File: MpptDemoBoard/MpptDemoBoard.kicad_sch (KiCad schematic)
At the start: 17 parts, among them IC1 SPV1040T, U1 282837-2, U2 282837-2

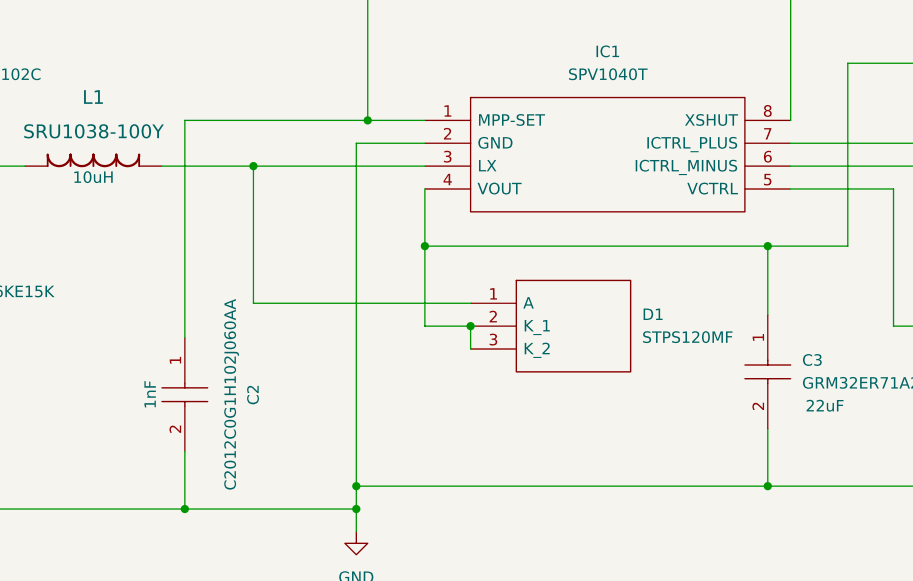
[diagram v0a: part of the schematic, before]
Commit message: Updated pcb with new diode
replaced diode STPS120MF (If=1A) with STPS2150A (If=2A). Updated symbol and footprint library and docs containing schematic, pcb layout image and 3d image.
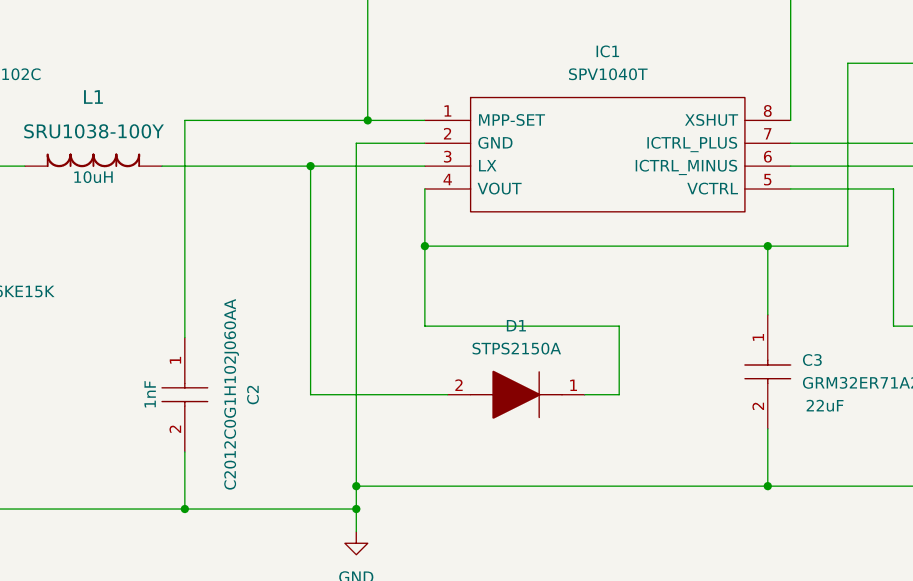
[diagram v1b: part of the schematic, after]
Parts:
- removed D1: STPS120MF, myfootprints:STPS120MF, symbol STPS120MF:STPS120MF
- added D1: STPS2150A, myfootprints:STPS2150A, symbol STPS2150A:STPS2150A
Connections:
- net at C3.1, IC1.4 (VOUT), R2.2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: now also D1.1
- net at IC1.3 (LX), L1.1: now also D1.2
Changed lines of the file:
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@@
   (junction (at 100.33 113.03) (diameter 0) (color 0 0 0 0)
   )
+  (junction (at 95.25 77.47) (diameter 0) (color 0 0 0 0)
+  )
   (junction (at 179.07 95.25) (diameter 0) (color 0 0 0 0)
   )
-  (junction (at 88.9 77.47) (diameter 0) (color 0 0 0 0)
-  )
   (junction (at 179.07 113.03) (diameter 0) (color 0 0 0 0)
   )
@@
   (junction (at 81.28 115.57) (diameter 0) (color 0 0 0 0)
   )
-  (junction (at 113.03 95.25) (diameter 0) (color 0 0 0 0)
-  )
   (junction (at 101.6 53.34) (diameter 0) (color 0 0 0 0)
   )
@@
     (stroke (width 0) (type default) (color 0 0 0 0))
   )
-  (wire (pts (xy 107.95 95.25) (xy 113.03 95.25))
-    (stroke (width 0) (type default) (color 0 0 0 0))
-  )
   (wire (pts (xy 148.59 80.01) (xy 160.02 80.01))
     (stroke (width 0) (type default) (color 0 0 0 0))
@@
     (stroke (width 0) (type default) (color 0 0 0 0))
   )
-  (wire (pts (xy 88.9 77.47) (xy 78.74 77.47))
+  (wire (pts (xy 78.74 77.47) (xy 95.25 77.47))
     (stroke (width 0) (type default) (color 0 0 0 0))
   )
@@
     (stroke (width 0) (type default) (color 0 0 0 0))
   )
+  (wire (pts (xy 129.54 102.87) (xy 125.73 102.87))
+    (stroke (width 0) (type default) (color 0 0 0 0))
+  )
   (wire (pts (xy 236.22 72.39) (xy 243.84 72.39))
     (stroke (width 0) (type default) (color 0 0 0 0))
@@
     (stroke (width 0) (type default) (color 0 0 0 0))
   )
+  (wire (pts (xy 95.25 77.47) (xy 95.25 102.87))
+    (stroke (width 0) (type default) (color 0 0 0 0))
+  )
   (wire (pts (xy 167.64 72.39) (xy 167.64 73.66))
     (stroke (width 0) (type default) (color 0 0 0 0))
@@
     (stroke (width 0) (type default) (color 0 0 0 0))
   )
+  (wire (pts (xy 110.49 102.87) (xy 95.25 102.87))
+    (stroke (width 0) (type default) (color 0 0 0 0))
+  )
   (wire (pts (xy 160.02 95.25) (xy 179.07 95.25))
     (stroke (width 0) (type default) (color 0 0 0 0))
@@
     (stroke (width 0) (type default) (color 0 0 0 0))
   )
-  (wire (pts (xy 88.9 92.71) (xy 88.9 77.47))
-    (stroke (width 0) (type default) (color 0 0 0 0))
-  )
   (wire (pts (xy 41.91 96.52) (xy 41.91 115.57))
     (stroke (width 0) (type default) (color 0 0 0 0))
@@
     (stroke (width 0) (type default) (color 0 0 0 0))
   )
-  (wire (pts (xy 113.03 92.71) (xy 88.9 92.71))
-    (stroke (width 0) (type default) (color 0 0 0 0))
-  )
   (wire (pts (xy 101.6 52.07) (xy 101.6 53.34))
     (stroke (width 0) (type default) (color 0 0 0 0))
@@
     (stroke (width 0) (type default) (color 0 0 0 0))
   )
-  (wire (pts (xy 113.03 95.25) (xy 113.03 97.79))
-    (stroke (width 0) (type default) (color 0 0 0 0))
-  )
   (wire (pts (xy 154.94 86.36) (xy 146.05 86.36))
     (stroke (width 0) (type default) (color 0 0 0 0))
@@
     (stroke (width 0) (type default) (color 0 0 0 0))
   )
-  (wire (pts (xy 107.95 77.47) (xy 88.9 77.47))
+  (wire (pts (xy 107.95 77.47) (xy 95.25 77.47))
     (stroke (width 0) (type default) (color 0 0 0 0))
   )
@@
     (stroke (width 0) (type default) (color 0 0 0 0))
   )
+  (wire (pts (xy 129.54 95.25) (xy 129.54 102.87))
+    (stroke (width 0) (type default) (color 0 0 0 0))
+  )
   (wire (pts (xy 41.91 125.73) (xy 41.91 115.57))
+    (stroke (width 0) (type default) (color 0 0 0 0))
+  )
+  (wire (pts (xy 107.95 95.25) (xy 129.54 95.25))
     (stroke (width 0) (type default) (color 0 0 0 0))
   )
@@
     (property "Datasheet" "" (id 3) (at 20.32 80.01 0)
       (effects (font (size 1.524 1.524)))
+    )
+    (pin "1")
+    (pin "2")
+  )
+  (symbol (lib_id "STPS2150A:STPS2150A") (at 125.73 102.87 180) (unit 1)
+    (in_bom yes) (on_board yes) (fields_autoplaced)
+    (property "Reference" "D1" (id 0) (at 118.11 95.25 0))
+    (property "Value" "STPS2150A" (id 1) (at 118.11 97.79 0))
+    (property "Footprint" "myfootprints:STPS2150A" (id 2) (at 114.3 102.87 0)
+      (effects (font (size 1.27 1.27)) (justify left) hide)
+    )
+    (property "Datasheet" "http://www.st.com/web/en/resource/technical/document/datasheet/CD00003322.pdf" (id 3) (at 114.3 100.33 0)
+      (effects (font (size 1.27 1.27)) (justify left) hide)
+    )
+    (property "Description" "STPS2150A, Schottky Diode,  2A max, 150V, 2-Pin, SMA" (id 4) (at 114.3 97.79 0)
+      (effects (font (size 1.27 1.27)) (justify left) hide)
+    )
+    (property "Height" "2.65" (id 5) (at 114.3 95.25 0)
+      (effects (font (size 1.27 1.27)) (justify left) hide)
+    )
+    (property "Mouser Part Number" "511-STPS2150A" (id 6) (at 114.3 92.71 0)
+      (effects (font (size 1.27 1.27)) (justify left) hide)
+    )
+    (property "Mouser Price/Stock" "https://www.mouser.co.uk/ProductDetail/STMicroelectronics/STPS2150A?qs=JV7lzlMm3yID2fZto%2F5JCQ%3D%3D" (id 7) (at 114.3 90.17 0)
+      (effects (font (size 1.27 1.27)) (justify left) hide)
+    )
+    (property "Manufacturer_Name" "STMicroelectronics" (id 8) (at 114.3 87.63 0)
+      (effects (font (size 1.27 1.27)) (justify left) hide)
+    )
+    (property "Manufacturer_Part_Number" "STPS2150A" (id 9) (at 114.3 85.09 0)
+      (effects (font (size 1.27 1.27)) (justify left) hide)
     )
     (pin "1")
@@
     (pin "2")
   )
-  (symbol (lib_id "STPS120MF:STPS120MF") (at 113.03 92.71 0) (unit 1)
-    (in_bom yes) (on_board yes) (fields_autoplaced)
-    (property "Reference" "D1" (id 0) (at 132.08 93.9799 0)
-      (effects (font (size 1.27 1.27)) (justify left))
-    )
-    (property "Value" "STPS120MF" (id 1) (at 132.08 96.5199 0)
-      (effects (font (size 1.27 1.27)) (justify left))
-    )
-    (property "Footprint" "myfootprints:STPS120MF" (id 2) (at 132.08 90.17 0)
-      (effects (font (size 1.27 1.27)) (justify left) hide)
-    )
-    (property "Datasheet" "https://www.st.com/resource/en/datasheet/stps120mf.pdf" (id 3) (at 132.08 92.71 0)
-      (effects (font (size 1.27 1.27)) (justify left) hide)
-    )
-    (property "Description" "Schottky Diodes & Rectifiers Power Schottky Rec 1A 20V 0.41VF" (id 4) (at 132.08 95.25 0)
-      (effects (font (size 1.27 1.27)) (justify left) hide)
-    )
-    (property "Height" "" (id 5) (at 132.08 97.79 0)
-      (effects (font (size 1.27 1.27)) (justify left) hide)
-    )
-    (property "Mouser Part Number" "511-STPS120MF" (id 6) (at 132.08 100.33 0)
-      (effects (font (size 1.27 1.27)) (justify left) hide)
-    )
-    (property "Mouser Price/Stock" "https://www.mouser.co.uk/ProductDetail/STMicroelectronics/STPS120MF?qs=vV0pr1uq7fBNdZQwvvztWg%3D%3D" (id 7) (at 132.08 102.87 0)
-      (effects (font (size 1.27 1.27)) (justify left) hide)
-    )
-    (property "Manufacturer_Name" "STMicroelectronics" (id 8) (at 132.08 105.41 0)
-      (effects (font (size 1.27 1.27)) (justify left) hide)
-    )
-    (property "Manufacturer_Part_Number" "STPS120MF" (id 9) (at 132.08 107.95 0)
-      (effects (font (size 1.27 1.27)) (justify left) hide)
-    )
-    (pin "1")
-    (pin "2")
-    (pin "3")
-  )
   (symbol (lib_id "C2012C0G1H102J060AA:C2012C0G1H102J060AA") (at 81.28 96.52 270) (unit 1)
     (in_bom yes) (on_board yes)
@@
       (reference "C5") (unit 1) (value "C2012C0G1H102J060AA") (footprint "myfootprints:C2012C0G1H102J060AA")
     )
-    (path "/c5ef3ad7-975e-4299-aab8-a87cbd45e466"
-      (reference "D1") (unit 1) (value "STPS120MF") (footprint "myfootprints:STPS120MF")
+    (path "/59268aa9-8315-40b4-96a6-9d7eab932b45"
+      (reference "D1") (unit 1) (value "STPS2150A") (footprint "myfootprints:STPS2150A")
     )
     (path "/a1dfbfca-1dc4-4899-b8bb-b26537771ef9"
